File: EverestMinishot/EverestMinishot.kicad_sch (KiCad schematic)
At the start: 3 parts, among them J1 Conn_01x03_Pin, SW1 Mode Switch, SW2 Camera Shutter

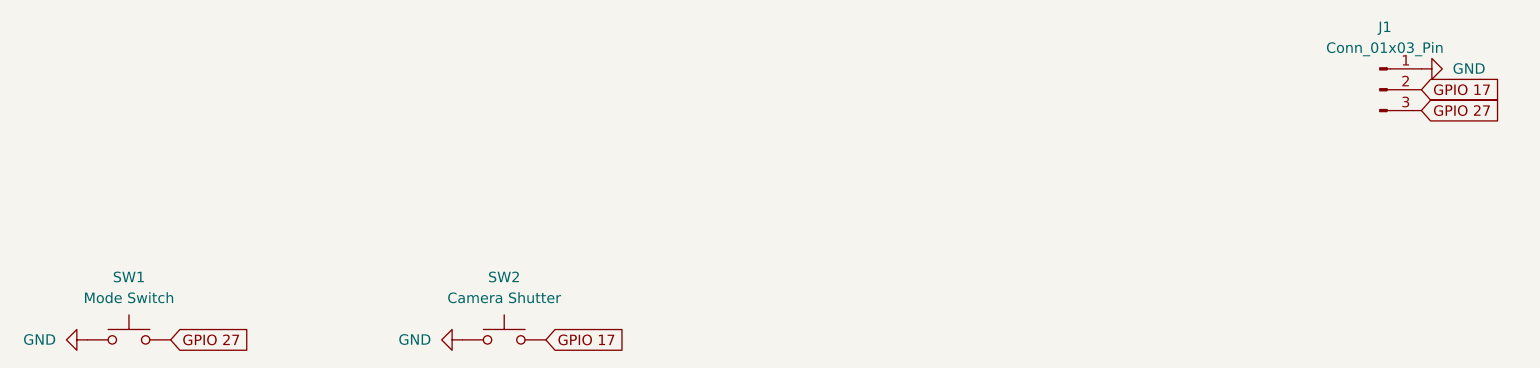
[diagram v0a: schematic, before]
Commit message: Made Code for Camera to work
In this update I made it so the camera would work using python code.
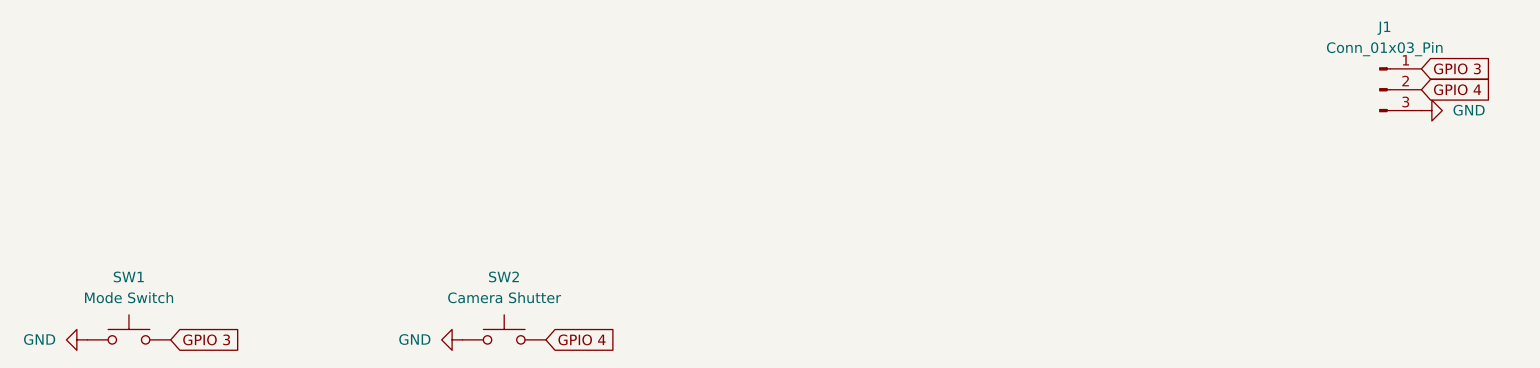
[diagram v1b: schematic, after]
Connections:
- net GND: now also J1.3 (Pin_3); no longer J1.1 (Pin_1)
- net GPIO 17 renamed GPIO 4
- net GPIO 27 renamed GPIO 3
- net GPIO 3: now also J1.1 (Pin_1); no longer J1.3 (Pin_3)
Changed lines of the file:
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@@
 	(generator_version "10.0")
 	(paper "A4")
-	(global_label "GPIO 27"
-		(shape input)
-		(at 228.6 91.44 0)
-		(fields_autoplaced yes)
-		(effects
-			(font
-				(size 1.27 1.27)
-			)
-			(justify left)
-		)
-		(property "Intersheetrefs" "${INTERSHEET_REFS}"
-			(at 239.4471 91.44 0)
-			(hide yes)
-			(show_name no)
-			(do_not_autoplace no)
-			(effects
-				(font
-					(size 1.27 1.27)
-				)
-				(justify left)
-			)
-		)
-	)
-	(global_label "GPIO 17"
+	(global_label "GPIO 4"
+		(shape input)
+		(at 228.6 88.9 0)
+		(fields_autoplaced yes)
+		(effects
+			(font
+				(size 1.27 1.27)
+			)
+			(justify left)
+		)
+		(property "Intersheetrefs" "${INTERSHEET_REFS}"
+			(at 238.2376 88.9 0)
+			(hide yes)
+			(show_name no)
+			(do_not_autoplace no)
+			(effects
+				(font
+					(size 1.27 1.27)
+				)
+				(justify left)
+			)
+		)
+	)
+	(global_label "GPIO 4"
 		(shape input)
 		(at 121.92 119.38 0)
@@
 		)
 		(property "Intersheetrefs" "${INTERSHEET_REFS}"
-			(at 132.7671 119.38 0)
-			(hide yes)
-			(show_name no)
-			(do_not_autoplace no)
-			(effects
-				(font
-					(size 1.27 1.27)
-				)
-				(justify left)
-			)
-		)
-	)
-	(global_label "GPIO 17"
-		(shape input)
-		(at 228.6 88.9 0)
-		(fields_autoplaced yes)
-		(effects
-			(font
-				(size 1.27 1.27)
-			)
-			(justify left)
-		)
-		(property "Intersheetrefs" "${INTERSHEET_REFS}"
-			(at 239.4471 88.9 0)
-			(hide yes)
-			(show_name no)
-			(do_not_autoplace no)
-			(effects
-				(font
-					(size 1.27 1.27)
-				)
-				(justify left)
-			)
-		)
-	)
-	(global_label "GPIO 27"
+			(at 131.5576 119.38 0)
+			(hide yes)
+			(show_name no)
+			(do_not_autoplace no)
+			(effects
+				(font
+					(size 1.27 1.27)
+				)
+				(justify left)
+			)
+		)
+	)
+	(global_label "GPIO 3"
+		(shape input)
+		(at 228.6 86.36 0)
+		(fields_autoplaced yes)
+		(effects
+			(font
+				(size 1.27 1.27)
+			)
+			(justify left)
+		)
+		(property "Intersheetrefs" "${INTERSHEET_REFS}"
+			(at 238.2376 86.36 0)
+			(hide yes)
+			(show_name no)
+			(do_not_autoplace no)
+			(effects
+				(font
+					(size 1.27 1.27)
+				)
+				(justify left)
+			)
+		)
+	)
+	(global_label "GPIO 3"
 		(shape input)
 		(at 76.2 119.38 0)
@@
 		)
 		(property "Intersheetrefs" "${INTERSHEET_REFS}"
-			(at 87.0471 119.38 0)
+			(at 85.8376 119.38 0)
 			(hide yes)
 			(show_name no)
@@
 	(symbol
 		(lib_id "power:GND")
-		(at 228.6 86.36 90)
+		(at 228.6 91.44 90)
 		(unit 1)
 		(body_style 1)
@@
 		(fields_autoplaced yes)
 		(property "Reference" "#PWR03"
-			(at 234.95 86.36 0)
+			(at 234.95 91.44 0)
 			(hide yes)
 			(show_name no)
@@
 		)
 		(property "Value" "GND"
-			(at 232.41 86.3599 90)
+			(at 232.41 91.4399 90)
 			(show_name no)
 			(do_not_autoplace no)
@@
 		)
 		(property "Footprint" ""
-			(at 228.6 86.36 0)
+			(at 228.6 91.44 0)
 			(hide yes)
 			(show_name no)
@@
 		)
 		(property "Datasheet" ""
-			(at 228.6 86.36 0)
+			(at 228.6 91.44 0)
 			(hide yes)
 			(show_name no)
@@
 		)
 		(property "Description" "Power symbol creates a global label with name \"GND\" , ground"
-			(at 228.6 86.36 0)
-			(hide yes)
-			(show_name no)
+			(at 228.6 91.44 0)
+			(hide yes)
+			(show_name no)
